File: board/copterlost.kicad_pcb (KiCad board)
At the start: 2 copper layers, 29.8 x 26 mm, 16 parts, among them J1 gnd, J2 5V_Copter, Q1 MMBT3904, SW1 SW_Push, U1 ATTINY13-20SSU

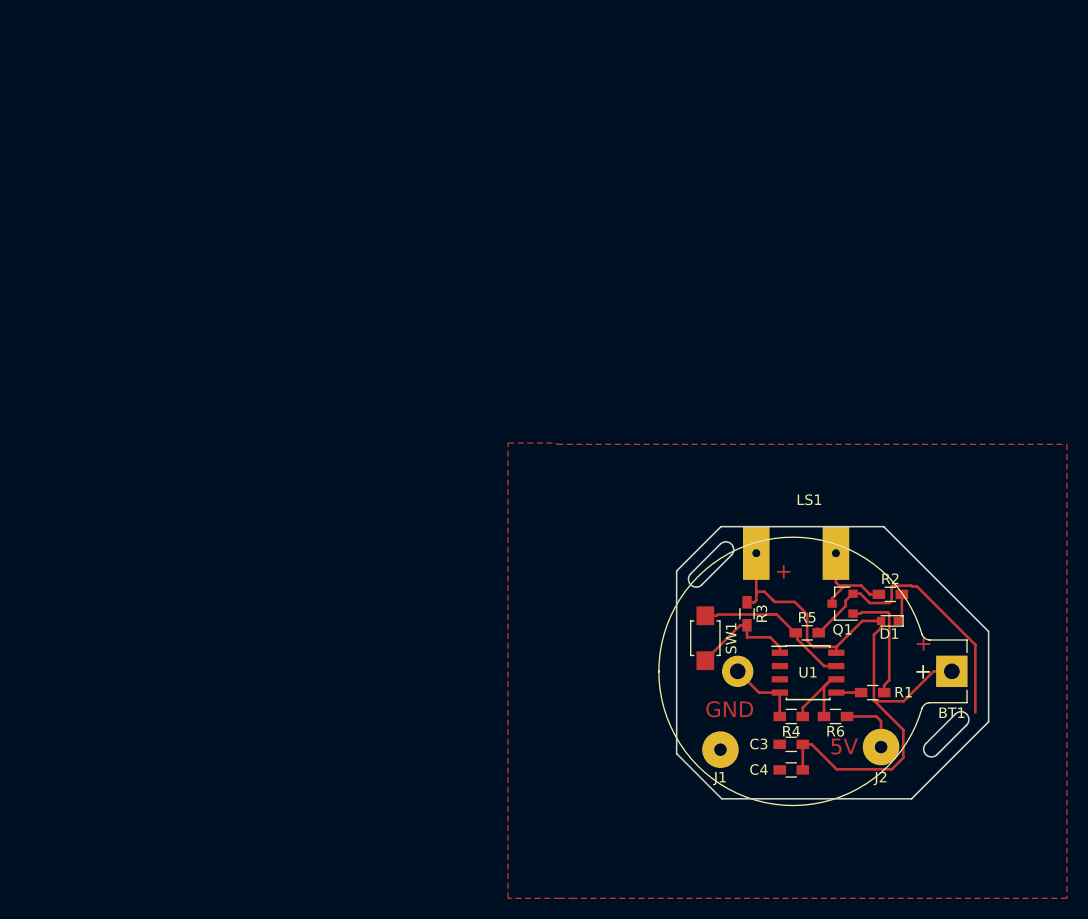
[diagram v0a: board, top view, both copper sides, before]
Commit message: migrate to kicad 5 & new layout
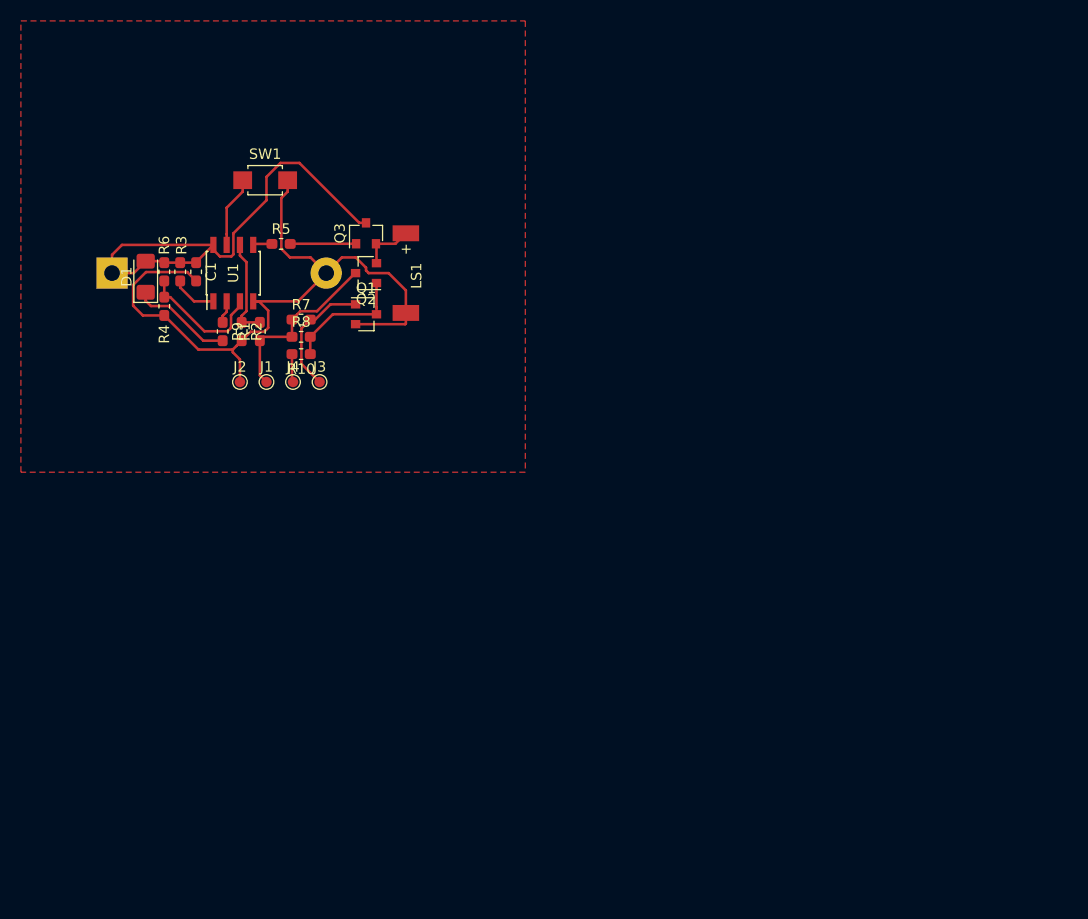
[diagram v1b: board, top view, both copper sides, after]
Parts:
- removed C3, C4: 0.1uF, Resistors_SMD:R_0603_HandSoldering
- added C1: 0.1uF, Capacitor_SMD:C_0603_1608Metric_Pad1.05x0.95mm_HandSolder, F.Cu at (113.3, 77.3)
- added J3: FC.Beeper-, TestPoint:TestPoint_Pad_D1.0mm, F.Cu at (125.1, 87.9)
- added J4: FC.Beeper+, TestPoint:TestPoint_Pad_D1.0mm, F.Cu at (122.6, 87.9)
- added Q2: MMBT3904, Package_TO_SOT_SMD:SOT-23, F.Cu at (129.5, 77.5)
- added Q3: MMBT3904, Package_TO_SOT_SMD:SOT-23, F.Cu at (129.5, 73.7)
- added R10: 5k, Resistor_SMD:R_0603_1608Metric_Pad1.05x0.95mm_HandSolder, F.Cu at (123.3, 85.2)
- added R7: 10k, Resistor_SMD:R_0603_1608Metric_Pad1.05x0.95mm_HandSolder, F.Cu at (123.3, 81.9)
- added R8: 5k, Resistor_SMD:R_0603_1608Metric_Pad1.05x0.95mm_HandSolder, F.Cu at (123.3, 83.6)
- added R9: 50, Resistor_SMD:R_0603_1608Metric_Pad1.05x0.95mm_HandSolder, F.Cu at (115.8, 83.1)
- BT1: footprint Battery_Holders:Keystone_104_1x23mm-CoinCell -> Battery:BatteryHolder_Keystone_104_1x23mm; moved to B.Cu
- D1: footprint LEDs:LED_0603 -> LED_SMD:LED_1206_3216Metric_Pad1.42x1.75mm_HandSolder
- J1: value gnd -> 5V_Copter; footprint Wire_Pads:SolderWirePad_single_1-2mmDrill -> TestPoint:TestPoint_Pad_D1.0mm
- J2: value 5V_Copter -> Ground; footprint Wire_Pads:SolderWirePad_single_1-2mmDrill -> TestPoint:TestPoint_Pad_D1.0mm
- LS1: footprint copterBeeper:beeper -> custom:Beeper
- Q1: footprint TO_SOT_Packages_SMD:SOT-23 -> Package_TO_SOT_SMD:SOT-23
- R1: value 560 -> 5k; footprint Resistors_SMD:R_0603_HandSoldering -> Resistor_SMD:R_0603_1608Metric_Pad1.05x0.95mm_HandSolder
- R2: value 100 -> 10k; footprint Resistors_SMD:R_0603_HandSoldering -> Resistor_SMD:R_0603_1608Metric_Pad1.05x0.95mm_HandSolder
- R3: value 1k -> 10k; footprint Resistors_SMD:R_0603_HandSoldering -> Resistor_SMD:R_0603_1608Metric_Pad1.05x0.95mm_HandSolder
- R4: value 10k -> 5k; footprint Resistors_SMD:R_0603_HandSoldering -> Resistor_SMD:R_0603_1608Metric_Pad1.05x0.95mm_HandSolder
- R5: value 10k -> 330; footprint Resistors_SMD:R_0603_HandSoldering -> Resistor_SMD:R_0603_1608Metric_Pad1.05x0.95mm_HandSolder
- R6: value 5k -> 10k; footprint Resistors_SMD:R_0603_HandSoldering -> Resistor_SMD:R_0603_1608Metric_Pad1.05x0.95mm_HandSolder
- SW1: footprint Buttons_Switches_SMD:SW_SPST_B3U-1000P -> custom:SW_SPST_B3U-1000P
- U1: footprint Housings_SOIC:SOIC-8_3.9x4.9mm_Pitch1.27mm -> Package_SO:SOIC-8_3.9x4.9mm_P1.27mm
- moved BT1 88.9 mm to (105.2, 77.5), turned to 0 degrees
- moved D1 78.4 mm to (108.5, 77.8), turned to 90 degrees
- moved R6 75.8 mm to (111.8, 77.3), turned to 90 degrees
- moved R4 71.7 mm to (110.2, 80.6), turned to 270 degrees
- moved J2 70.6 mm to (117.5, 87.9)
- moved R1 68.1 mm to (119.4, 83.1), turned to 90 degrees
- moved U1 67.0 mm to (116.8, 77.5), turned to 90 degrees
- moved R2 67.0 mm to (117.6, 83.1), turned to 270 degrees
- moved R3 64.6 mm to (110.2, 77.3)
- moved R5 62.6 mm to (121.4, 74.7)
- moved SW1 60.8 mm to (119.9, 68.6), turned to 0 degrees
- moved J1 55.9 mm to (120.0, 87.9), turned to 0 degrees
- moved Q1 53.3 mm to (129.5, 81.4), turned to 0 degrees
- moved LS1 41.4 mm to (133.3, 77.5), turned to 90 degrees
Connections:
- BT1 pad 1: Net-(BT1-Pad1) -> +BATT
- D1 pad 2: Net-(BT1-Pad1) -> +BATT
- J1 pad 1: GND -> +5V
- J2 pad 1: Net-(J2-Pad1) -> GND
- LS1 pad 1: Net-(BT1-Pad1) -> /Speaker
- LS1 pad 2: Net-(LS1-Pad2) -> GND
- Q1 pad 1: Net-(Q1-Pad1) -> Net-(J3-Pad1)
- Q1 pad 3: Net-(LS1-Pad2) -> Net-(Q1-Pad3)
- R1 pad 1: Net-(Q1-Pad1) -> +5V
- R1 pad 2: Net-(R1-Pad2) -> /Sense
- R2 pad 1: Net-(LS1-Pad2) -> /Sense
- R2 pad 2: Net-(D1-Pad1) -> GND
- R3 pad 1: Net-(BT1-Pad1) -> +BATT
- R3 pad 2: Net-(R3-Pad2) -> /Batt-Sense
- R4 pad 1: Net-(R4-Pad1) -> /Batt-Sense
- R5 pad 2: GND -> /Beeper
- R6 pad 1: Net-(J2-Pad1) -> Net-(R6-Pad1)
- R6 pad 2: Net-(R4-Pad1) -> +BATT
- SW1 pad 1: Net-(R5-Pad1) -> /Button
- SW1 pad 2: Net-(R3-Pad2) -> GND
- U1 pad 1: Net-(R3-Pad2) -> Net-(R6-Pad1)
- U1 pad 2: (no net) -> /LED
- U1 pad 3: (no net) -> /Batt-Sense
- U1 pad 5: Net-(R1-Pad2) -> Net-(R5-Pad1)
- U1 pad 6: Net-(R4-Pad1) -> /Sense
- U1 pad 7: Net-(R5-Pad1) -> /Button
- U1 pad 8: Net-(BT1-Pad1) -> +BATT
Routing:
- net Net-(BT1-Pad1): track 59.9 -> 0.00 mm
- net +BATT: track 0.00 -> 46.8 mm
- net GND: track 35.9 -> 69.1 mm
- net +5V: track 0.00 -> 17.0 mm
- net Net-(R5-Pad1): track 15.8 -> 1.83 mm
- net /Batt-Sense: track 0.00 -> 12.3 mm
- net Net-(J3-Pad1): track 0.00 -> 12.0 mm
- net Net-(Q1-Pad3): track 0.00 -> 11.9 mm
- net Net-(Q1-Pad1): track 11.3 -> 0.00 mm
- net Net-(R3-Pad2): track 10.6 -> 0.00 mm
- net Net-(R4-Pad1): track 10.3 -> 0.00 mm
- net Net-(LS1-Pad2): track 9.61 -> 0.00 mm
- net /Sense: track 0.00 -> 9.60 mm
- net Net-(D1-Pad1): track 2.70 -> 9.76 mm
- net /Button: track 0.00 -> 6.87 mm
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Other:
- board outline removed
- net class Default: clearance 0.254 -> 0.2; trace_width 0.254 -> 0.25; via_dia 0.6 -> 0.8
- rule pad_to_mask_clearance: 0.2 -> 0
- rule trace_clearance: 0.254 -> 0.2
- board text removed: "+"
- board text removed: "5V"
- board text removed: "GND"

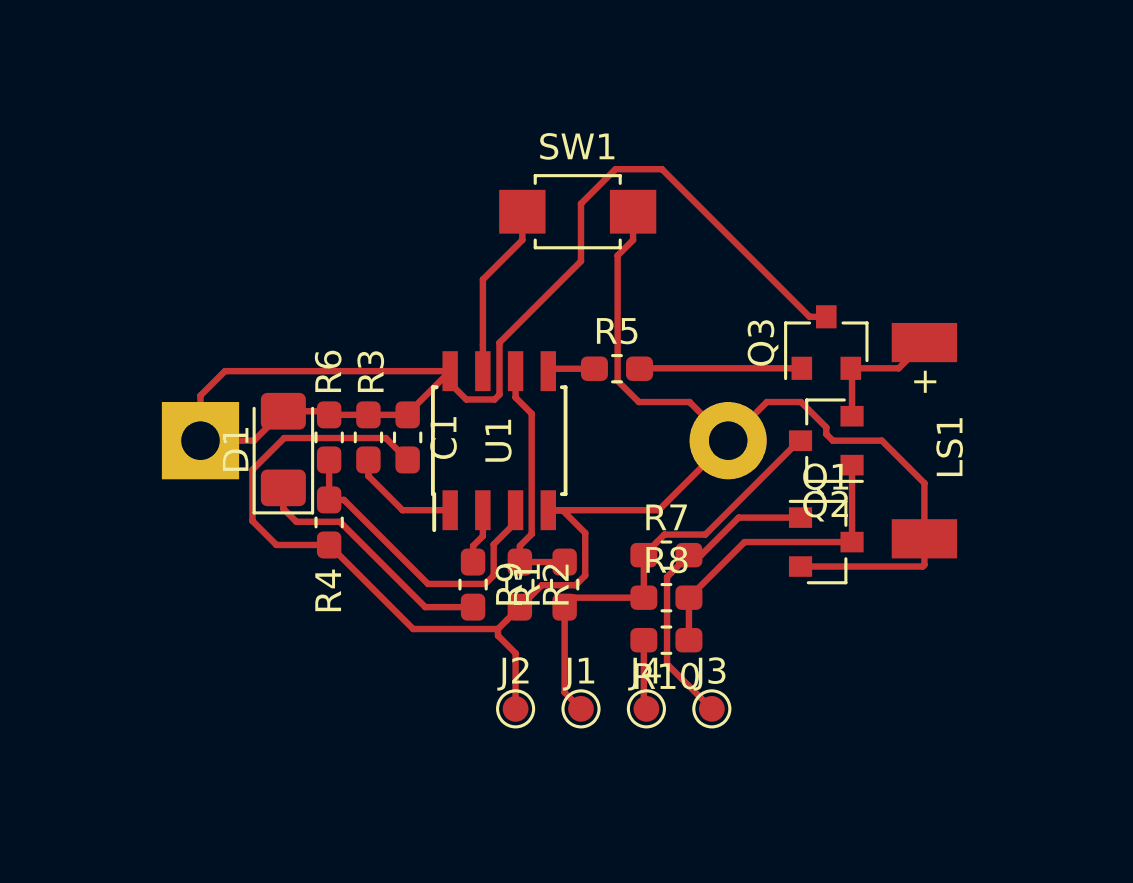
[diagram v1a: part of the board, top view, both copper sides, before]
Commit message: squeeze to smaller layout
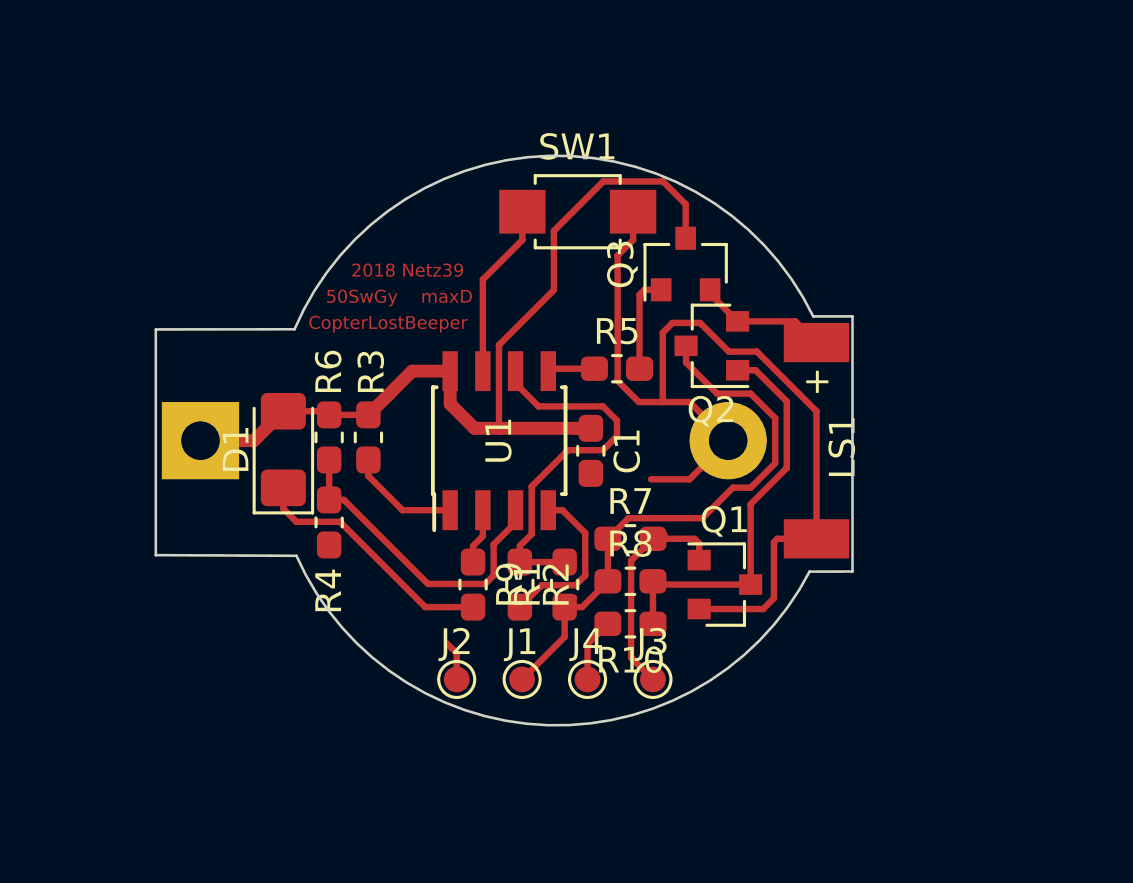
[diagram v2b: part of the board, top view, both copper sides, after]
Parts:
- moved C1 7.13 mm to (120.4, 77.9)
- moved Q3 6.25 mm to (124.1, 70.6)
- moved Q2 5.77 mm to (125.1, 73.8)
- moved Q1 4.27 mm to (125.6, 83.1)
- moved LS1 4.19 mm to (129.2, 77.5)
- moved J1 2.56 mm to (117.7, 86.7)
- moved J2 2.56 mm to (115.2, 86.7)
- moved J3 2.56 mm to (122.8, 86.7)
- moved J4 2.56 mm to (120.3, 86.7)
- moved R10 1.53 mm to (121.9, 84.6)
- moved R7 1.53 mm to (121.9, 81.3)
- moved R8 1.53 mm to (121.9, 82.9)
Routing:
- net GND: track 69.1 -> 45.9 mm
- net +BATT: track 46.8 -> 37.2 mm
- net +5V: track 17.0 -> 22.2 mm
- net /Sense: track 9.60 -> 14.6 mm
- net Net-(Q1-Pad3): track 11.9 -> 15.9 mm
- net /Beeper: track 6.31 -> 3.82 mm
- net Net-(J3-Pad1): track 12.0 -> 9.63 mm
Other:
- board outline added: 27.1 x 22.1 mm
- board text added: "2018 Netz39"
- board text added: "50SwGy"
- board text added: "CopterLostBeeper"
- board text added: "maxD"

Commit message: ready to etch
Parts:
- added REF**: OSHW-Logo_5.7x6mm_Copper, Symbol:OSHW-Logo_5.7x6mm_Copper, F.Cu at (114.3, 71.4)
- R3: value 10k -> 18k
